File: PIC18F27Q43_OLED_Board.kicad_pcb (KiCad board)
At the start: 2 copper layers, 55 parts, among them J1 Conn_PIC_ICSP_ICD, J2 OLED_Connector, J4 USB_B_Mini, Q1 C143946, SW1 SW_Push, SW2 SW_Push, SW3 SW_Push, SW4 SW_Push, SW5 SW_SPDT, U1 PIC18F27Q43-I/STX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

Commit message: Rev.1 : PCB Design finished.
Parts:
- removed BT1: V, Battery:BatteryHolder_ComfortableElectronic_CH273-2450_1x2450
- moved R5 60.0 mm to (139.6, 111.1), turned to 90 degrees
- moved R1 58.2 mm to (94.5, 111.6), turned to 90 degrees
- moved R19 58.0 mm to (145.5, 111.0), turned to -90 degrees
- moved R15 58.0 mm to (100.5, 111.1), turned to -90 degrees
- moved R17 57.8 mm to (136.0, 111.0), turned to -90 degrees
- moved R4 56.7 mm to (130.0, 111.1), turned to 90 degrees
- moved R16 54.3 mm to (111.0, 111.0), turned to -90 degrees
- moved R18 52.3 mm to (141.9, 103.5)
- moved R3 52.0 mm to (105.0, 111.5), turned to 90 degrees
- moved D11 51.8 mm to (97.5, 112.1)
- moved R20 49.3 mm to (141.9, 105.5)
- moved J4 47.6 mm to (146.8, 93.0), turned to 90 degrees
- moved R2 45.8 mm to (134.0, 88.0), turned to 90 degrees
- moved D10 44.1 mm to (106.0, 84.5), turned to -90 degrees
- moved D12 40.9 mm to (108.0, 112.1)
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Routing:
- net VCC: track 0.00 -> 100.1 mm
- net GND: track 0.00 -> 59.1 mm, vias 0 -> 8
- net Net-(SW5-B): track 0.00 -> 52.5 mm, vias 0 -> 1
- net /RB4: track 0.00 -> 49.3 mm, vias 0 -> 2
- net /RB3: track 0.00 -> 38.0 mm, vias 0 -> 2
- net /RB5: track 0.00 -> 36.7 mm, vias 0 -> 2
- net /RB1: track 0.00 -> 32.1 mm
- net /RC7: track 0.00 -> 31.3 mm, vias 0 -> 2
- net /MCLR: track 0.00 -> 30.5 mm, vias 0 -> 2
- net /RB2: track 0.00 -> 28.5 mm, vias 0 -> 2
- net /PGD: track 0.00 -> 25.3 mm, vias 0 -> 2
- net /RC2: track 0.00 -> 24.6 mm
- net /PGC: track 0.00 -> 23.7 mm
- net /RC6: track 0.00 -> 23.7 mm, vias 0 -> 2
- net /RB0: track 0.00 -> 23.6 mm, vias 0 -> 2
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- added copper zone on F.Cu, net GND
- added copper zone on B.Cu, net VCC
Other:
- board outline added: 57.5 x 40 mm
- board text added: "GND"
- board text added: "ICSP"
- board text added: "KiCAD"
- board text added: "Made with"
- board text added: "OLED Board PIC18F27Q43 Rev.1: 28th March 2025 Designed by @deulamco"
- board text added: "SCK/SCL"
- board text added: "SDA"
- board text added: "VCC"

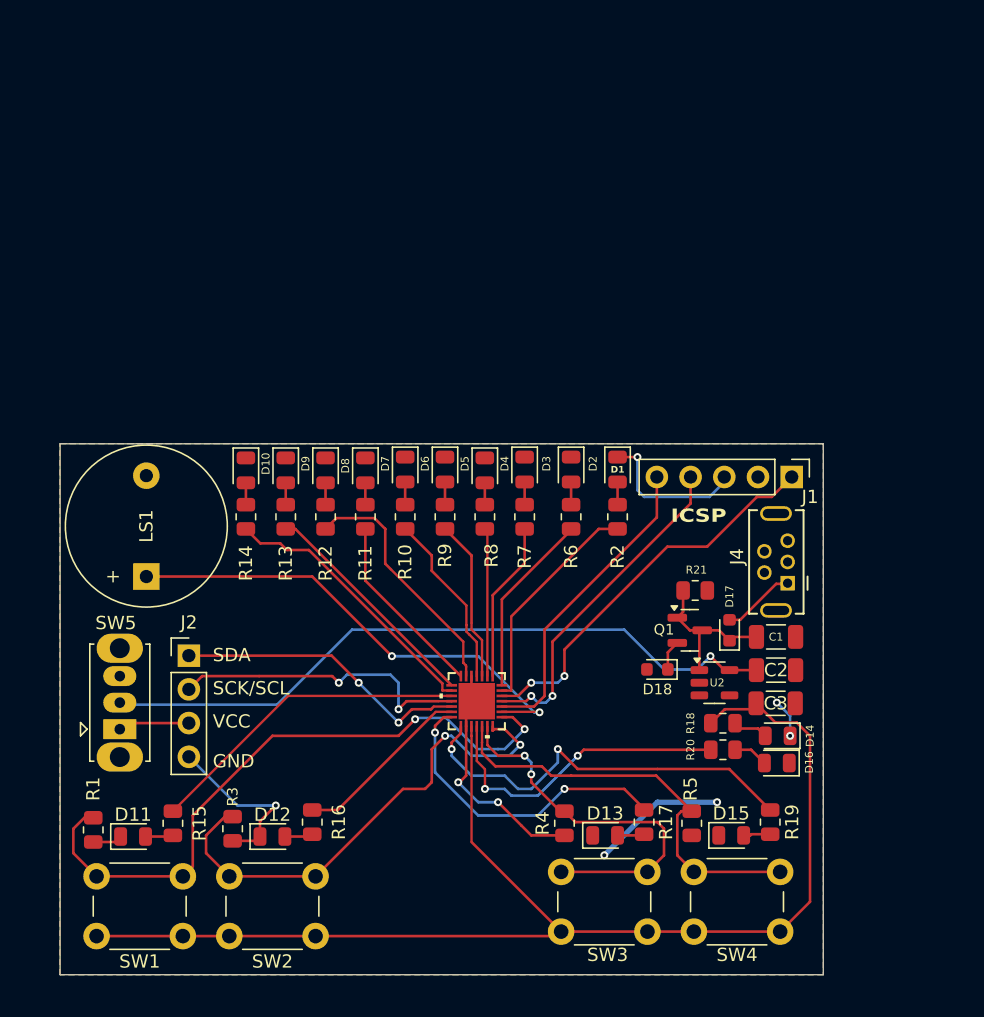
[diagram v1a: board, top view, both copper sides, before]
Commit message: Refine Silkscreen
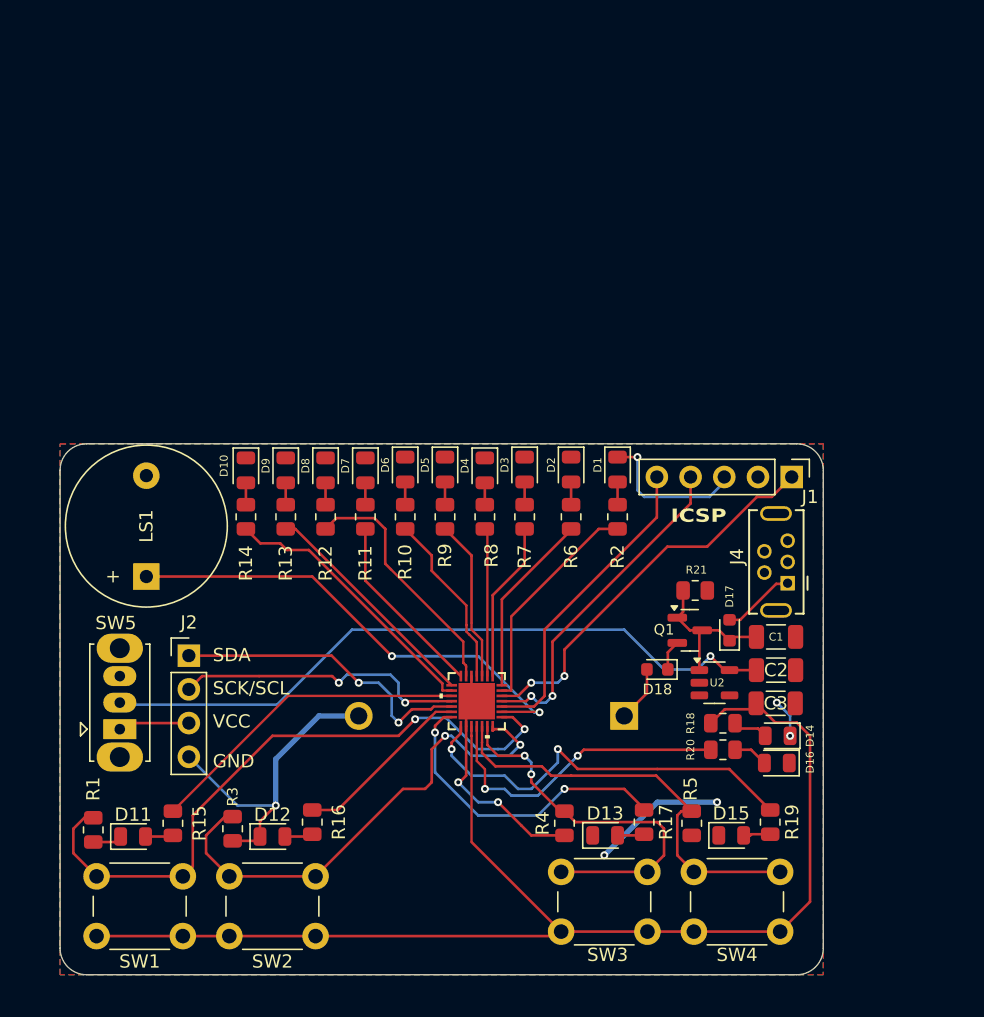
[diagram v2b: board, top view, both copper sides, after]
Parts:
- added BT1: V, Battery:BatteryHolder_ComfortableElectronic_CH273-2450_1x2450, B.Cu at (134.5, 103.0)
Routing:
- net GND: track 59.1 -> 70.2 mm
- net Net-(BT1-+): track 0.00 -> 4.21 mm
- net /SCL: track 23.2 -> 22.2 mm
- net /SDA: track 22.4 -> 23.3 mm
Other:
- outline, holes or cut-outs redrawn

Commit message: move from Q43 -> Q84 due to chip shortage
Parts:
- U1: footprint PIC18F27Q43-I-STX:VQFN28_STX_MCH -> PIC18F27Q84-I-SN:VQFN28_5N_MCH-L

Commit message: Finished Routing to new Q84
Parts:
- moved U1 1.01 mm to (123.7, 101.0)
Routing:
- net Net-(SW5-B): track 52.5 -> 63.5 mm
- net /SCL: track 22.2 -> 28.2 mm, vias 2 -> 0
- net /RA0: track 17.0 -> 14.4 mm
- net /SDA: track 23.3 -> 20.6 mm, vias 2 -> 0
- net GND: track 70.2 -> 67.6 mm
- net /RA2: track 12.1 -> 9.84 mm
- net /RA6: track 14.1 -> 12.1 mm
- net /RA1: track 13.9 -> 12.1 mm
- net /RA7: track 18.8 -> 16.9 mm
- net /RB5: track 36.7 -> 38.5 mm
- net /RA5: track 13.3 -> 11.7 mm
- net /RA4: track 12.2 -> 10.7 mm
- net /RA3: track 11.2 -> 9.73 mm
- net /RC1: track 20.9 -> 19.4 mm
- net /RB3: track 38.0 -> 36.8 mm
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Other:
- board text added: "OLED Board PIC18F27Q84 Rev.2: 28th March 2025 Designed by @deulamco"
- board text removed: "OLED Board PIC18F27Q43 Rev.1: 28th March 2025 Designed by @deulamco"
